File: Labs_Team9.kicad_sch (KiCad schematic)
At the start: 38 parts, among them J1 Conn_02x04_Counter_Clockwise, J2 Conn_01x03_Pin, J3 Conn_01x04_Pin, J4 Conn_01x04_Pin, SW1 SW_Push, SW2 SW_Push, SW3 SW_Push, SW4 SW_Push, SW5 SW_Push, SW6 SW_Push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

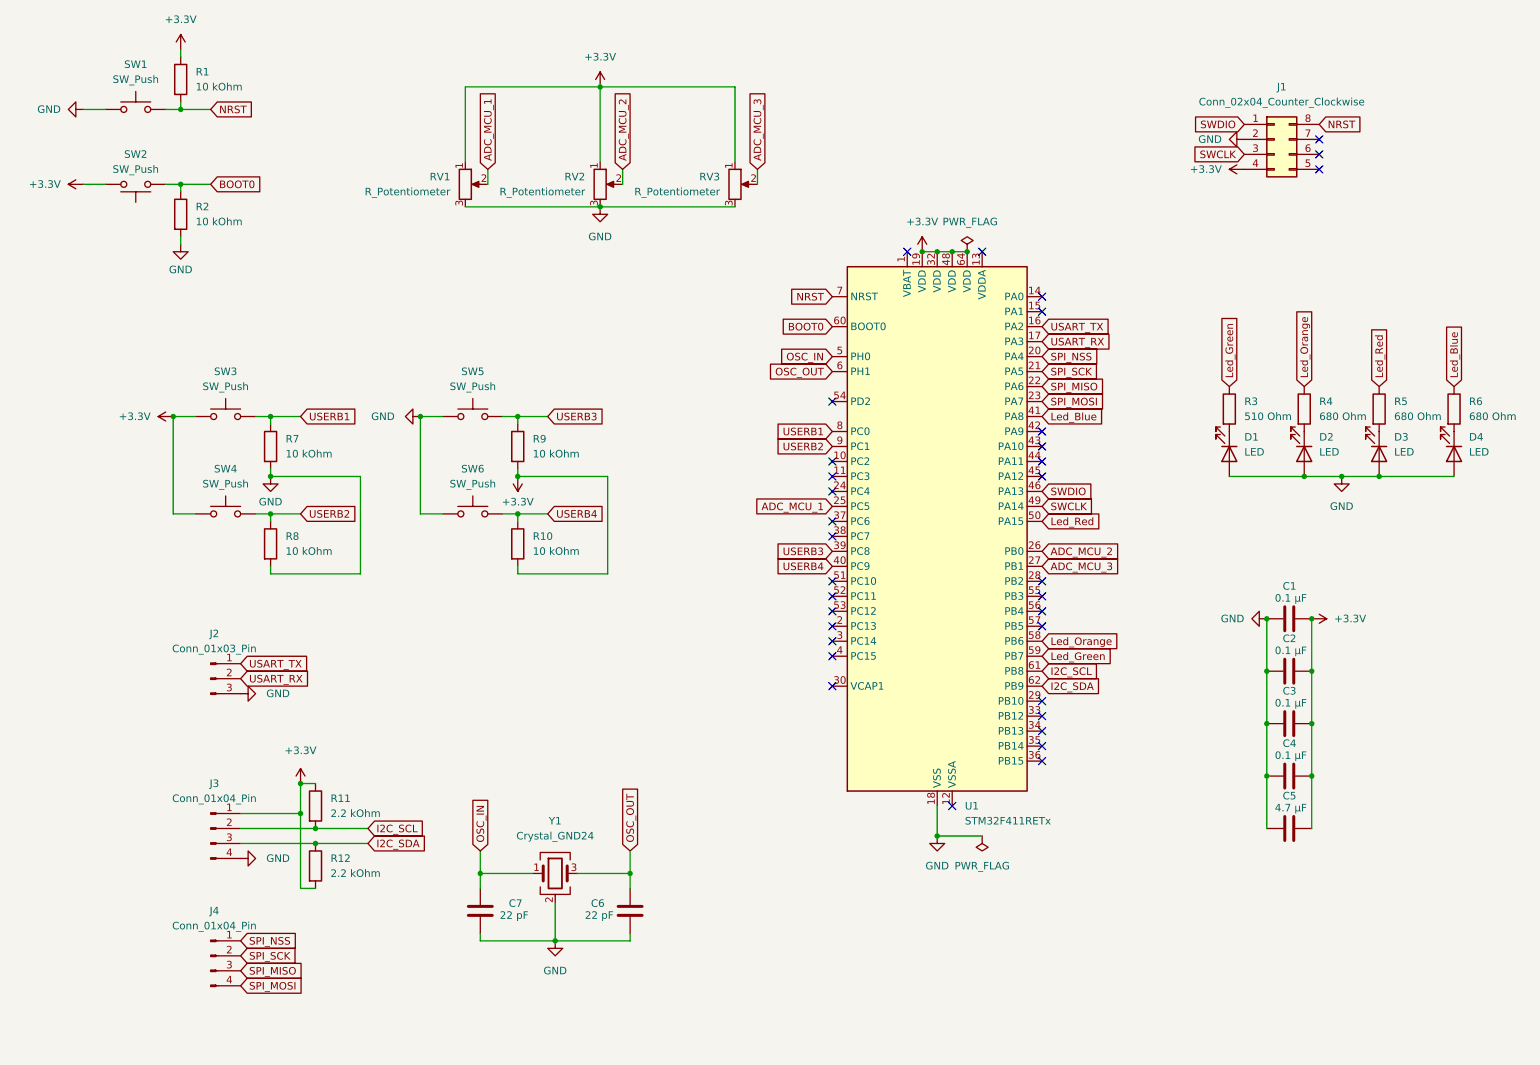
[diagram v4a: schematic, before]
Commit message: lab4: add schematic and tracing
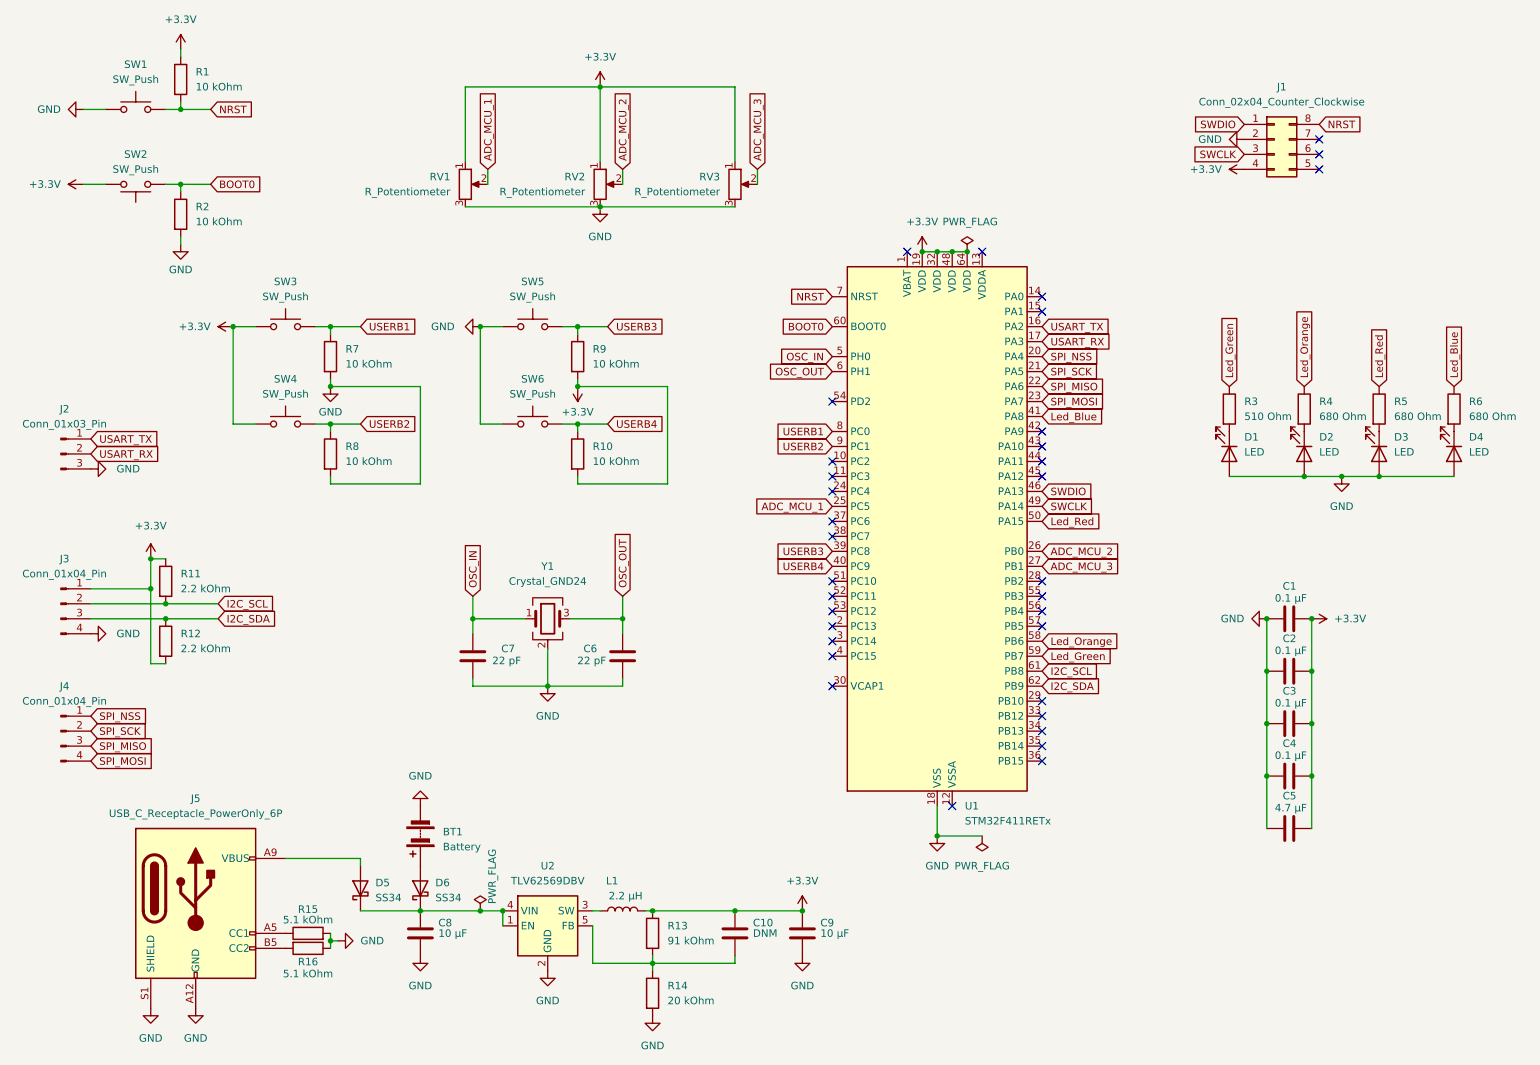
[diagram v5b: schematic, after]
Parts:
- added BT1: Battery, Battery:BatteryHolder_Keystone_2479_3xAAA, symbol Device:Battery
- added C10: DNM, Capacitor_SMD:C_1206_3216Metric_Pad1.33x1.80mm_HandSolder, symbol Device:C
- added C8, C9: 10 μF, Capacitor_SMD:C_1206_3216Metric_Pad1.33x1.80mm_HandSolder, symbol Device:C
- added D5, D6: SS34, Diode_SMD:D_SMA_Handsoldering, symbol Diode:SS34
- added J5: USB_C_Receptacle_PowerOnly_6P, Connector_USB:USB_C_Receptacle_GCT_USB4135-GF-A_6P_TopMnt_Horizontal, symbol Connector:USB_C_Receptacle_PowerOnly_6P
- added L1: 2.2 μH, Inductor_SMD:L_0805_2012Metric_Pad1.05x1.20mm_HandSolder, symbol Device:L
- added R13: 91 kOhm, Resistor_SMD:R_1206_3216Metric_Pad1.30x1.75mm_HandSolder, symbol Device:R
- added R14: 20 kOhm, Resistor_SMD:R_1206_3216Metric_Pad1.30x1.75mm_HandSolder, symbol Device:R
- added R15, R16: 5.1 kOhm, Resistor_SMD:R_1206_3216Metric_Pad1.30x1.75mm_HandSolder, symbol Device:R
- added U2: TLV62569DBV, Package_TO_SOT_SMD:SOT-23-5, symbol Regulator_Switching:TLV62569DBV
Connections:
- net +3.3V: now also C10.1, C9.1, L1.2, R13.1
- net GND: now also BT1.2 (-), C8.2, C9.2, J5.A12 (GND), J5.B12 (GND), J5.S1 (SHIELD), R14.2, R15.2, R16.1, U2.2 (GND)
- new net: C8.1, D5.1 (K), D6.1 (K), U2.1 (EN), U2.4 (VIN)
- new net: L1.1, U2.3 (SW)
- new net: C10.2, R13.2, R14.1, U2.5 (FB)
- new net: J5.A5 (CC1), R15.1
- new net: D5.2 (A), J5.A9 (VBUS), J5.B9 (VBUS)
- new net: J5.B5 (CC2), R16.2
- new net: BT1.1 (+), D6.2 (A)
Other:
- moved on the sheet: C6, C7, J2, J3, J4, R10, R11, R12, R7, R8, R9, SW3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
